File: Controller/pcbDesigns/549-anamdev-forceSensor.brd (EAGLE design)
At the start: 53 x 54 mm, 42 parts, among them IC1 REG1117, J2 AVR_SPI_PROG_3X2PTH, J3 POWER_JACK, Q1 MMBT4403, U1 328P, U2 HX711

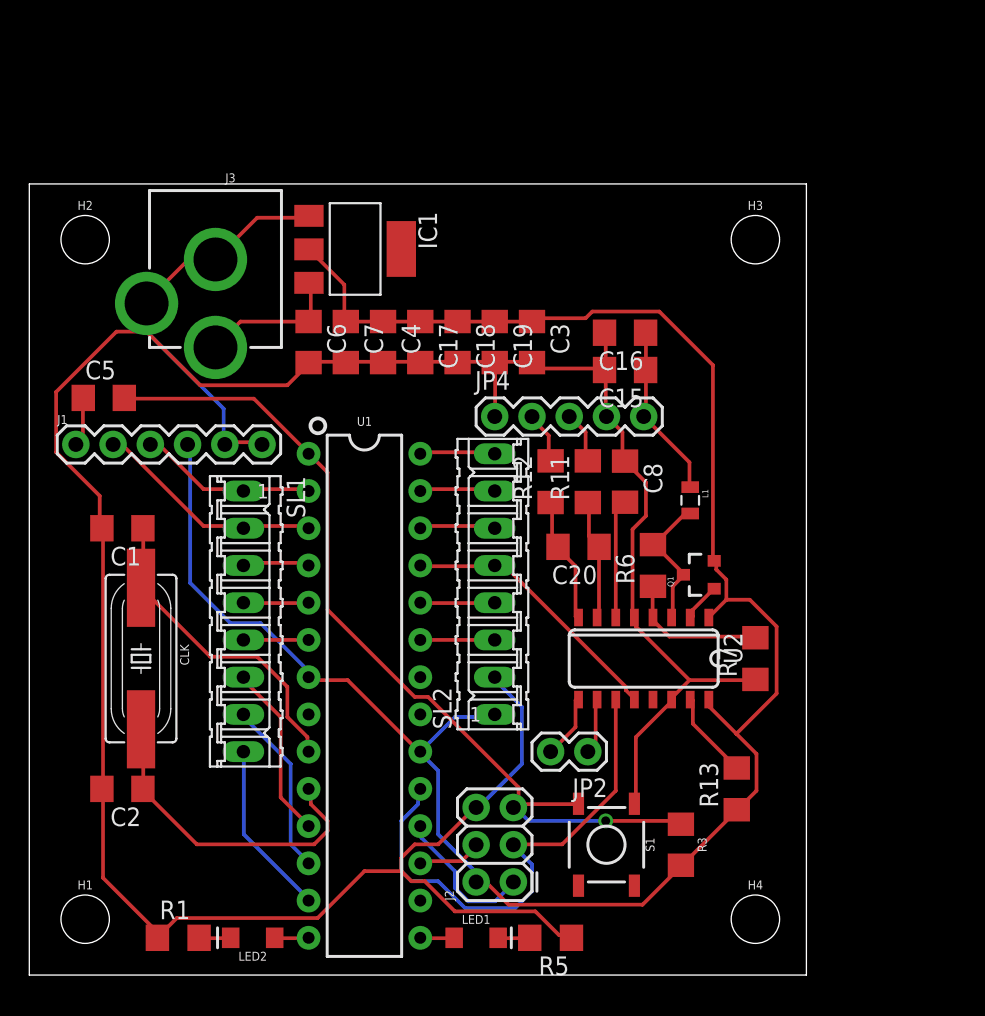
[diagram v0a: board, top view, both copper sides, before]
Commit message: added multiple amplifiers for force sensor
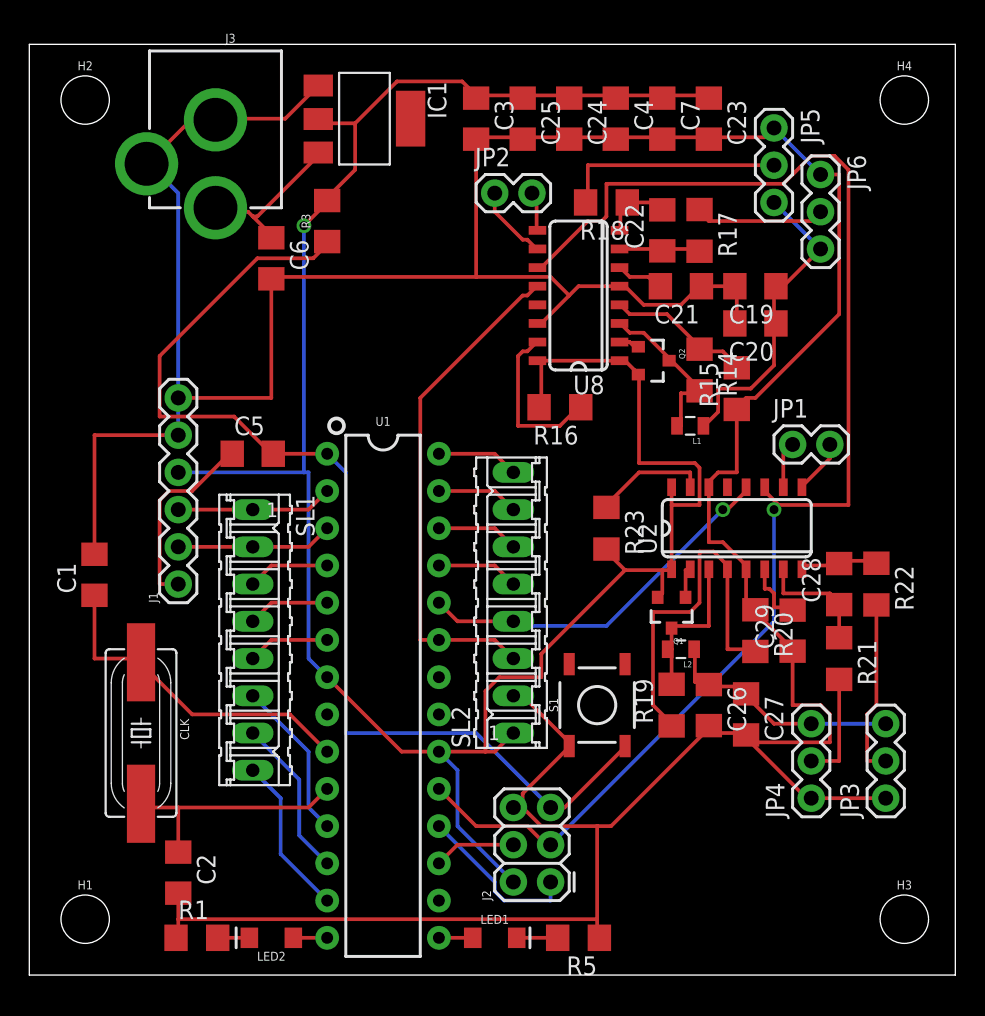
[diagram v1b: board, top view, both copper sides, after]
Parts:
- removed C15: .1 uF, rcl:C1206
- removed C16: 10uF, rcl:C1206
- removed C17, C18, C8: 0.1uF, rcl:C1206
- removed R11, R12: 100, rcl:R1206
- removed R13: 10K, rcl:R1206
- removed R6: 20k, rcl:R1206
- removed R7: 8.2k, rcl:R1206
- added C21, C22, C23, C24, C26, C28, C29: 0.1uF, rcl:C1206
- added C25, C27: 10uF, rcl:C1206
- added JP1: (no value), SparkFun-Connectors:1X02
- added JP3, JP5: LL, SparkFun-Connectors:1X03
- added JP6: LR, SparkFun-Connectors:1X03
- added L2: 3.3uH, SparkFun-Passives:0805
- added Q2: MMBT4403, SparkFun-DiscreteSemi:SOT23-3
- added R14: 20k, rcl:R1206
- added R15: 8.2k, rcl:R1206
- added R16, R23: 10k, rcl:R1206
- added R17, R18, R21, R22: 100, rcl:R1206
- added R19, R20: 330, rcl:R1206
- added U8: HX711, Testing:SO16
- C19: value 10uF -> 0.1uF
- C20: value 0.1uF -> 10uF
- JP4: value (none) -> LR; device SparkFun-Connectors:1X05 -> SparkFun-Connectors:1X03
- moved H4 56.8 mm to (59.7, 59.7)
- moved R3 48.9 mm to (20.3, 51.4), turned to 90 degrees
- moved H3 47.5 mm to (59.7, 3.81)
- moved JP2 38.6 mm to (31.8, 53.3), turned to 0 degrees
- moved JP4 33.8 mm to (53.3, 12.1), turned to 90 degrees
- moved C7 26.4 mm to (43.2, 58.4)
- moved C4 22.0 mm to (40.0, 58.4)
- moved C20 19.4 mm to (49.5, 44.5)
- moved C19 18.2 mm to (49.5, 47.0), turned to 180 degrees
- moved C3 15.7 mm to (30.5, 58.4)
- moved J1 11.8 mm to (10.2, 26.7), turned to 90 degrees
- moved U2 10.9 mm to (48.3, 30.5), turned to 0 degrees
- moved C5 10.9 mm to (15.2, 35.6)
- moved S1 9.55 mm to (38.7, 18.4), turned to 90 degrees
- moved J3 9.53 mm to (12.7, 66.0)
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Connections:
- removed net A+: JP4.2, R12.2
- removed net A-: JP4.3, R11.2
- removed net AVDD: C15.1, C16.1, JP4.5, L1.1
- removed net B+: JP2.1, U2.10
- removed net B-: JP2.2, U2.9
- new net A+0: JP5.2, R18.2
- new net A+1: JP3.2, R22.2
- new net A-0: JP6.2, R17.1
- new net A-1: JP4.2, R21.2
- new net AVDD0: C19.1, C20.1, JP5.3, JP6.3, L1.1
- new net AVDD1: C26.1, C27.1, JP3.3, JP4.3, L2.1
- new net B+0: JP2.1, U8.10
- new net B+1: JP1.1, U2.10
- new net B-0: JP2.2, U8.9
- new net B-1: JP1.2, U2.9
- new net N$13: C21.2, U8.6
- new net N$16: L1.2, Q2.3, R14.2, U8.3
- new net N$19: C22.2, R18.1, U8.8
- new net N$6: Q2.1, U8.2
- new net N$8: R14.1, R15.2, U8.4
- new net PC0: SL2.3, U1.23, U8.12
- new net PC1: SL2.4, U1.24, U2.12
- net GND: now also C20.2, C21.1, C23.2, C24.2, C25.2, C26.2, C27.2, C29.1, JP3.1, JP5.1, JP6.1, R15.1, R20.1, U8.14, U8.5; no longer C15.2, C16.2, C17.2, C18.2, C8.1, JP4.4, R7.1
- net N$17: now also R16.1, U8.15; no longer SL2.4, U1.24
- net N$18: now also C22.1, R17.2, U8.7; no longer SL2.3, U1.23
- net N$23: now also R19.1, R20.2; no longer R6.1, R7.2
- net N$24: now also C29.2; no longer C8.2
- net N$25: now also L2.2, R19.2; no longer L1.2, R6.2
- net N$26: now also R23.1; no longer R13.2
- net N$27: now also C28.1, R21.1; no longer C20.1, R11.1
- net N$28: now also C28.2, R22.1; no longer C20.2, R12.1
- net PC2: no longer U2.12
- net SCK: now also U8.11
- net VCC: now also C23.1, C24.1, C25.1, Q2.2, R16.2, R23.2, U8.1, U8.16; no longer C17.1, C18.1, C19.1, R13.1
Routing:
- net GND: track 209.5 -> 274.2 mm
- net SCK: track 35.0 -> 94.1 mm, vias 0 -> 1
- net PC0: track 0.00 -> 34.5 mm
- net PC1: track 0.00 -> 25.9 mm, vias 0 -> 1
- net AVDD0: track 0.00 -> 21.7 mm
- net VCC: track 141.1 -> 160.6 mm, vias 0 -> 1
- net AVDD1: track 0.00 -> 16.8 mm
- net N$23: track 9.82 -> 25.3 mm
- net A+0: track 0.00 -> 15.4 mm
- net PC2: track 18.6 -> 5.61 mm
- net RESET: track 61.4 -> 73.9 mm, vias 1 -> 0
- net A+1: track 0.00 -> 12.2 mm
- net AVDD: track 11.9 -> 0.00 mm
- net N$16: track 0.00 -> 11.5 mm
- net N$8: track 0.00 -> 10.1 mm
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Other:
- board size 53 x 54 mm -> 63.2 x 63.5 mm

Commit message: updated pcb boards
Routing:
- net AVDD0: track 21.7 -> 8.08 mm
- net N$24: track 4.50 -> 0.00 mm
- net N$13: track 3.31 -> 0.00 mm
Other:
- board text added: "Team15"
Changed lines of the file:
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@@
 <wire x1="63.17" y1="63.49" x2="0" y2="63.49" width="0" layer="20"/>
 <wire x1="0" y1="63.49" x2="0" y2="0" width="0" layer="20"/>
+<text x="41.91" y="5.08" size="2.54" layer="1" font="vector" ratio="16">Team15</text>
 </plain>
 <attributes>
@@
 <wire x1="45.72" y1="42.545" x2="45.72" y2="42.697" width="0.254" layer="1"/>
 </signal>
-<signal name="N$13">
-<contactref element="U8" pad="6"/>
-<contactref element="C21" pad="2"/>
-<wire x1="40.9575" y1="47.625" x2="40.3225" y2="48.26" width="0.254" layer="1"/>
-<wire x1="42.2275" y1="47.625" x2="40.9575" y2="47.625" width="0.254" layer="1"/>
-<wire x1="42.8625" y1="46.99" x2="42.2275" y2="47.625" width="0.254" layer="1"/>
-<wire x1="40.3225" y1="48.26" x2="40.265" y2="48.26" width="0.254" layer="1"/>
-<wire x1="42.8625" y1="46.99" x2="43.05" y2="46.99" width="0.254" layer="1"/>
-</signal>
 <signal name="N$16">
 <contactref element="Q2" pad="3"/>
@@
 </signal>
 <signal name="AVDD1">
-<contactref element="L2" pad="1"/>
 <contactref element="JP3" pad="3"/>
 <contactref element="JP4" pad="3"/>
+<wire x1="50.8" y1="17.145" x2="48.895" y2="19.05" width="0.254" layer="1"/>
+<wire x1="53.34" y1="17.145" x2="50.8" y2="17.145" width="0.254" layer="1"/>
+<wire x1="53.34" y1="17.145" x2="58.42" y2="17.145" width="0.254" layer="16"/>
+<contactref element="L2" pad="1"/>
 <contactref element="C27" pad="1"/>
 <contactref element="C26" pad="1"/>
@@
 <wire x1="46.355" y1="20.0025" x2="45.4025" y2="20.0025" width="0.254" layer="1"/>
 <wire x1="45.4025" y1="22.225" x2="45.35" y2="22.225" width="0.254" layer="1"/>
-<wire x1="46.355" y1="20.0025" x2="46.355" y2="19.815" width="0.254" layer="1"/>
 <wire x1="48.5775" y1="19.685" x2="48.895" y2="19.3675" width="0.254" layer="1"/>
 <wire x1="46.355" y1="19.685" x2="48.5775" y2="19.685" width="0.254" layer="1"/>
 <wire x1="48.895" y1="19.3675" x2="48.895" y2="19.18" width="0.254" layer="1"/>
-<wire x1="46.355" y1="19.685" x2="46.355" y2="19.815" width="0.254" layer="1"/>
-<wire x1="50.8" y1="17.145" x2="48.895" y2="19.05" width="0.254" layer="1"/>
-<wire x1="53.34" y1="17.145" x2="50.8" y2="17.145" width="0.254" layer="1"/>
-<wire x1="48.895" y1="19.05" x2="48.895" y2="19.18" width="0.254" layer="1"/>
-<wire x1="53.34" y1="17.145" x2="58.42" y2="17.145" width="0.254" layer="16"/>
+<wire x1="48.895" y1="19.18" x2="48.895" y2="19.05" width="0" layer="19" extent="1-1"/>
+<wire x1="46.355" y1="19.815" x2="46.355" y2="19.685" width="0" layer="19" extent="1-1"/>
+<wire x1="46.355" y1="20.0025" x2="46.355" y2="19.815" width="0" layer="19" extent="1-1"/>
 </signal>
 <signal name="N$20">
@@
 <wire x1="47.625" y1="27.94" x2="47.625" y2="27.68" width="0.254" layer="1"/>
 </signal>
-<signal name="N$24">
-<contactref element="U2" pad="6"/>
-<contactref element="C29" pad="2"/>
-<wire x1="50.165" y1="26.3525" x2="50.165" y2="27.68" width="0.254" layer="1"/>
-<wire x1="50.4825" y1="26.3525" x2="50.165" y2="26.3525" width="0.254" layer="1"/>
-<wire x1="50.8" y1="26.035" x2="50.4825" y2="26.3525" width="0.254" layer="1"/>
-<wire x1="50.8" y1="25.0825" x2="50.8" y2="26.035" width="0.254" layer="1"/>
-<wire x1="52.07" y1="25.0825" x2="50.8" y2="25.0825" width="0.254" layer="1"/>
-<wire x1="52.07" y1="25.0825" x2="52.07" y2="24.895" width="0.254" layer="1"/>
-</signal>
 <signal name="N$25">
 <contactref element="Q1" pad="3"/>
@@
 </signal>
 <signal name="AVDD0">
-<contactref element="L1" pad="1"/>
 <contactref element="JP5" pad="3"/>
 <contactref element="JP6" pad="3"/>
+<wire x1="53.975" y1="49.53" x2="50.8" y2="52.705" width="0.254" layer="16"/>
+<wire x1="51.435" y1="46.99" x2="53.975" y2="49.53" width="0.254" layer="1"/>
+<contactref element="L1" pad="1"/>
+<contactref element="C20" pad="1"/>
 <contactref element="C19" pad="1"/>
-<contactref element="C20" pad="1"/>
-<wire x1="53.975" y1="49.53" x2="50.8" y2="52.705" width="0.254" layer="16"/>
-<wire x1="46.99" y1="38.4175" x2="46.0375" y2="37.465" width="0.254" layer="1"/>
-<wire x1="46.99" y1="40.005" x2="46.99" y2="38.4175" width="0.254" layer="1"/>
-<wire x1="49.2125" y1="40.005" x2="46.99" y2="40.005" width="0.254" layer="1"/>
-<wire x1="50.8" y1="41.5925" x2="49.2125" y2="40.005" width="0.254" layer="1"/>
-<wire x1="50.8" y1="44.45" x2="50.8" y2="41.5925" width="0.254" layer="1"/>
-<wire x1="46.0375" y1="37.465" x2="45.985" y2="37.465" width="0.254" layer="1"/>
-<wire x1="50.8" y1="44.45" x2="50.8" y2="46.99" width="0.254" layer="1"/>
-<wire x1="50.8" y1="46.99" x2="50.93" y2="46.99" width="0.254" layer="1"/>
-<wire x1="50.8" y1="44.45" x2="50.93" y2="44.45" width="0.254" layer="1"/>
-<wire x1="51.435" y1="46.99" x2="53.975" y2="49.53" width="0.254" layer="1"/>
-<wire x1="50.93" y1="46.99" x2="51.435" y2="46.99" width="0.254" layer="1"/>
+<wire x1="50.93" y1="46.99" x2="51.435" y2="46.99" width="0" layer="19" extent="1-1"/>
+<wire x1="50.93" y1="44.45" x2="50.93" y2="46.99" width="0" layer="19" extent="1-1"/>
+<wire x1="45.985" y1="37.465" x2="50.93" y2="44.45" width="0" layer="19" extent="1-1"/>
 </signal>
 <signal name="A-1">
@@
 <wire x1="34.6075" y1="49.53" x2="34.665" y2="49.53" width="0.254" layer="1"/>
 </signal>
+<signal name="N$13">
+<contactref element="U8" pad="6"/>
+<contactref element="C21" pad="2"/>
+<wire x1="43.05" y1="46.99" x2="40.265" y2="48.26" width="0" layer="19" extent="1-1"/>
+</signal>
+<signal name="N$24">
+<contactref element="U2" pad="6"/>
+<contactref element="C29" pad="2"/>
+<wire x1="52.07" y1="24.895" x2="50.165" y2="27.68" width="0" layer="19" extent="1-1"/>
+</signal>
 </signals>

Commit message: fixed issues with pcb
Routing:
- net AVDD0: track 8.08 -> 28.0 mm, vias 0 -> 1
- net N$24: track 0.00 -> 3.71 mm
- net N$13: track 0.00 -> 3.31 mm
- net AVDD1: track 16.4 -> 17.1 mm
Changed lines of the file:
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@@
 <contactref element="JP3" pad="3"/>
 <contactref element="JP4" pad="3"/>
-<wire x1="50.8" y1="17.145" x2="48.895" y2="19.05" width="0.254" layer="1"/>
+<wire x1="50.8" y1="17.145" x2="48.9458" y2="18.9992" width="0.254" layer="1"/>
+<wire x1="48.9458" y1="18.9992" x2="48.895" y2="19.05" width="0.254" layer="1"/>
 <wire x1="53.34" y1="17.145" x2="50.8" y2="17.145" width="0.254" layer="1"/>
 <wire x1="53.34" y1="17.145" x2="58.42" y2="17.145" width="0.254" layer="16"/>
@@
 <contactref element="C26" pad="1"/>
 <wire x1="45.4025" y1="20.0025" x2="45.4025" y2="22.225" width="0.254" layer="1"/>
-<wire x1="46.355" y1="20.0025" x2="45.4025" y2="20.0025" width="0.254" layer="1"/>
+<wire x1="46.355" y1="20.0025" x2="46.1772" y2="20.0025" width="0.254" layer="1"/>
+<wire x1="46.1772" y1="20.0025" x2="45.4025" y2="20.0025" width="0.254" layer="1"/>
 <wire x1="45.4025" y1="22.225" x2="45.35" y2="22.225" width="0.254" layer="1"/>
 <wire x1="48.5775" y1="19.685" x2="48.895" y2="19.3675" width="0.254" layer="1"/>
-<wire x1="46.355" y1="19.685" x2="48.5775" y2="19.685" width="0.254" layer="1"/>
+<wire x1="46.355" y1="19.685" x2="46.4058" y2="19.685" width="0.254" layer="1"/>
+<wire x1="46.4058" y1="19.685" x2="48.5775" y2="19.685" width="0.254" layer="1"/>
 <wire x1="48.895" y1="19.3675" x2="48.895" y2="19.18" width="0.254" layer="1"/>
-<wire x1="48.895" y1="19.18" x2="48.895" y2="19.05" width="0" layer="19" extent="1-1"/>
-<wire x1="46.355" y1="19.815" x2="46.355" y2="19.685" width="0" layer="19" extent="1-1"/>
-<wire x1="46.355" y1="20.0025" x2="46.355" y2="19.815" width="0" layer="19" extent="1-1"/>
+<wire x1="46.1772" y1="19.8882" x2="46.1772" y2="20.0025" width="0.254" layer="1"/>
+<wire x1="46.1772" y1="19.8882" x2="46.355" y2="19.815" width="0.254" layer="1"/>
+<wire x1="46.4058" y1="19.6596" x2="46.355" y2="19.815" width="0.254" layer="1"/>
+<wire x1="46.4058" y1="19.6596" x2="46.4058" y2="19.685" width="0.254" layer="1"/>
+<wire x1="48.9204" y1="18.9738" x2="48.895" y2="19.18" width="0.254" layer="1"/>
+<wire x1="48.9204" y1="18.9738" x2="48.9458" y2="18.9992" width="0.254" layer="1"/>
 </signal>
 <signal name="N$20">
@@
 <contactref element="JP6" pad="3"/>
 <wire x1="53.975" y1="49.53" x2="50.8" y2="52.705" width="0.254" layer="16"/>
-<wire x1="51.435" y1="46.99" x2="53.975" y2="49.53" width="0.254" layer="1"/>
+<wire x1="51.435" y1="46.99" x2="51.4858" y2="47.0408" width="0.254" layer="1"/>
 <contactref element="L1" pad="1"/>
 <contactref element="C20" pad="1"/>
 <contactref element="C19" pad="1"/>
-<wire x1="50.93" y1="46.99" x2="51.435" y2="46.99" width="0" layer="19" extent="1-1"/>
-<wire x1="50.93" y1="44.45" x2="50.93" y2="46.99" width="0" layer="19" extent="1-1"/>
-<wire x1="45.985" y1="37.465" x2="50.93" y2="44.45" width="0" layer="19" extent="1-1"/>
+<wire x1="51.4858" y1="47.0408" x2="53.975" y2="49.53" width="0.254" layer="1"/>
+<wire x1="50.9778" y1="46.863" x2="50.9778" y2="44.577" width="0.254" layer="1"/>
+<wire x1="50.9778" y1="44.577" x2="50.93" y2="44.45" width="0.254" layer="1"/>
+<wire x1="50.9778" y1="46.863" x2="50.93" y2="46.99" width="0.254" layer="1"/>
+<wire x1="47.0916" y1="37.2618" x2="46.1772" y2="37.2618" width="0.254" layer="1"/>
+<wire x1="47.3202" y1="37.0332" x2="47.0916" y2="37.2618" width="0.254" layer="1"/>
+<wire x1="47.3202" y1="42.7482" x2="47.3202" y2="37.0332" width="0.254" layer="16"/>
+<wire x1="53.9496" y1="49.3776" x2="47.3202" y2="42.7482" width="0.254" layer="16"/>
+<wire x1="46.1772" y1="37.2618" x2="45.985" y2="37.465" width="0.254" layer="1"/>
+<wire x1="53.9496" y1="49.3776" x2="53.975" y2="49.53" width="0.254" layer="16"/>
+<wire x1="51.435" y1="47.0916" x2="50.9778" y2="47.0916" width="0.254" layer="1"/>
+<wire x1="50.9778" y1="47.0916" x2="50.93" y2="46.99" width="0.254" layer="1"/>
+<wire x1="51.435" y1="47.0916" x2="51.4858" y2="47.0408" width="0.254" layer="1"/>
+<via x="47.3202" y="37.0332" extent="1-16" drill="0.6096"/>
 </signal>
 <signal name="A-1">
@@
 <contactref element="U8" pad="6"/>
 <contactref element="C21" pad="2"/>
-<wire x1="43.05" y1="46.99" x2="40.265" y2="48.26" width="0" layer="19" extent="1-1"/>
+<wire x1="41.8338" y1="48.2346" x2="40.4622" y2="48.2346" width="0.254" layer="1"/>
+<wire x1="42.9768" y1="47.0916" x2="41.8338" y2="48.2346" width="0.254" layer="1"/>
+<wire x1="40.4622" y1="48.2346" x2="40.265" y2="48.26" width="0.254" layer="1"/>
+<wire x1="42.9768" y1="47.0916" x2="43.05" y2="46.99" width="0.254" layer="1"/>
 </signal>
 <signal name="N$24">
 <contactref element="U2" pad="6"/>
 <contactref element="C29" pad="2"/>
-<wire x1="52.07" y1="24.895" x2="50.165" y2="27.68" width="0" layer="19" extent="1-1"/>
+<wire x1="50.292" y1="26.5176" x2="50.292" y2="27.6606" width="0.254" layer="1"/>
+<wire x1="51.8922" y1="24.9174" x2="50.292" y2="26.5176" width="0.254" layer="1"/>
+<wire x1="50.292" y1="27.6606" x2="50.165" y2="27.68" width="0.254" layer="1"/>
+<wire x1="51.8922" y1="24.9174" x2="52.07" y2="24.895" width="0.254" layer="1"/>
 </signal>
 </signals>
